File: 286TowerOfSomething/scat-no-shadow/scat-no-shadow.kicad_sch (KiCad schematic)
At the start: 1 part, among them J1 Bus_ISA_16bit

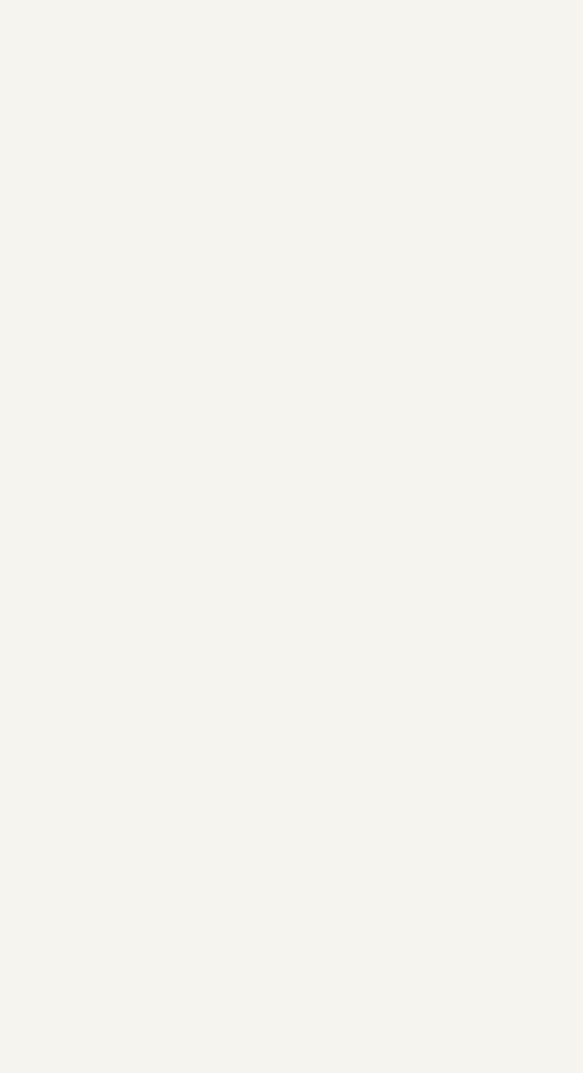
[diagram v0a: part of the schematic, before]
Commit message: Added symbol for 286 CPU, and associated datasheet
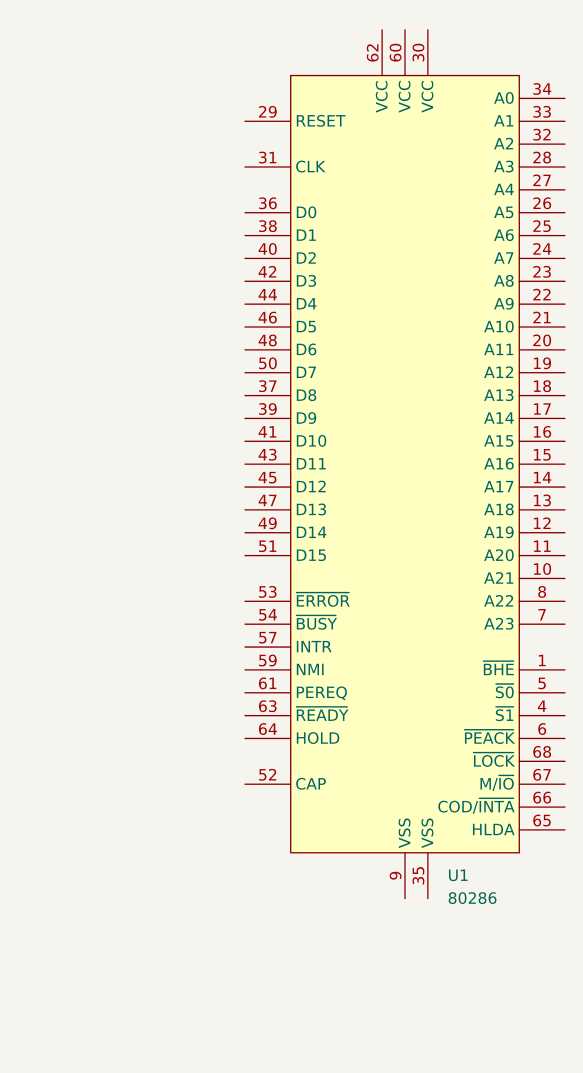
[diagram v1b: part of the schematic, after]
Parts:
- added U1: 80286, Package_LCC:PLCC-68_THT-Socket, symbol pc-parts:80286
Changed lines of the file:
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@@
 	(paper "A4")
+	(symbol
+		(lib_id "pc-parts:80286")
+		(at 129.54 86.36 0)
+		(unit 1)
+		(exclude_from_sim no)
+		(in_bom yes)
+		(on_board yes)
+		(dnp no)
+		(fields_autoplaced yes)
+		(property "Reference" "U1"
+			(at 134.2741 132.08 0)
+			(effects
+				(font
+					(size 1.27 1.27)
+				)
+				(justify left)
+			)
+		)
+		(property "Value" "80286"
+			(at 134.2741 134.62 0)
+			(effects
+				(font
+					(size 1.27 1.27)
+				)
+				(justify left)
+			)
+		)
+		(property "Footprint" "Package_LCC:PLCC-68_THT-Socket"
+			(at 129.54 86.36 0)
+			(effects
+				(font
+					(size 1.27 1.27)
+				)
+				(hide yes)
+			)
+		)
+		(property "Datasheet" ""
+			(at 129.54 86.36 0)
+			(effects
+				(font
+					(size 1.27 1.27)
+				)
+				(hide yes)
+			)
+		)
+		(property "Description" ""
+			(at 129.54 86.36 0)
+			(effects
+				(font
+					(size 1.27 1.27)
+				)
+				(hide yes)
+			)
+		)
+		(pin "59"
+		)
+		(pin "29"
+		)
+		(pin "44"
+		)
+		(pin "65"
+		)
+		(pin "38"
+		)
+		(pin "27"
+		)
+		(pin "6"
+		)
+		(pin "5"
+		)
+		(pin "51"
+		)
+		(pin "52"
+		)
+		(pin "53"
+		)
+		(pin "12"
+		)
+		(pin "40"
+		)
+		(pin "26"
+		)
+		(pin "9"
+		)
+		(pin "48"
+		)
+		(pin "34"
+		)
+		(pin "68"
+		)
+		(pin "37"
+		)
+		(pin "8"
+		)
+		(pin "62"
+		)
+		(pin "20"
+		)
+		(pin "64"
+		)
+		(pin "54"
+		)
+		(pin "4"
+		)
+		(pin "61"
+		)
+		(pin "63"
+		)
+		(pin "35"
+		)
+		(pin "66"
+		)
+		(pin "43"
+		)
+		(pin "46"
+		)
+		(pin "7"
+		)
+		(pin "57"
+		)
+		(pin "30"
+		)
+		(pin "32"
+		)
+		(pin "45"
+		)
+		(pin "36"
+		)
+		(pin "50"
+		)
+		(pin "39"
+		)
+		(pin "24"
+		)
+		(pin "18"
+		)
+		(pin "28"
+		)
+		(pin "17"
+		)
+		(pin "31"
+		)
+		(pin "60"
+		)
+		(pin "21"
+		)
+		(pin "33"
+		)
+		(pin "23"
+		)
+		(pin "25"
+		)
+		(pin "19"
+		)
+		(pin "22"
+		)
+		(pin "15"
+		)
+		(pin "11"
+		)
+		(pin "10"
+		)
+		(pin "16"
+		)
+		(pin "41"
+		)
+		(pin "1"
+		)
+		(pin "13"
+		)
+		(pin "47"
+		)
+		(pin "49"
+		)
+		(pin "42"
+		)
+		(pin "14"
+		)
+		(pin "67"
+		)
+		(instances
+			(project ""
+				(path "/1307a1c5-eee1-43f5-b6e9-638f413fecd9"
+					(reference "U1")
+					(unit 1)
+				)
+			)
+		)
+	)
 	(symbol
 		(lib_id "Connector:Bus_ISA_16bit")

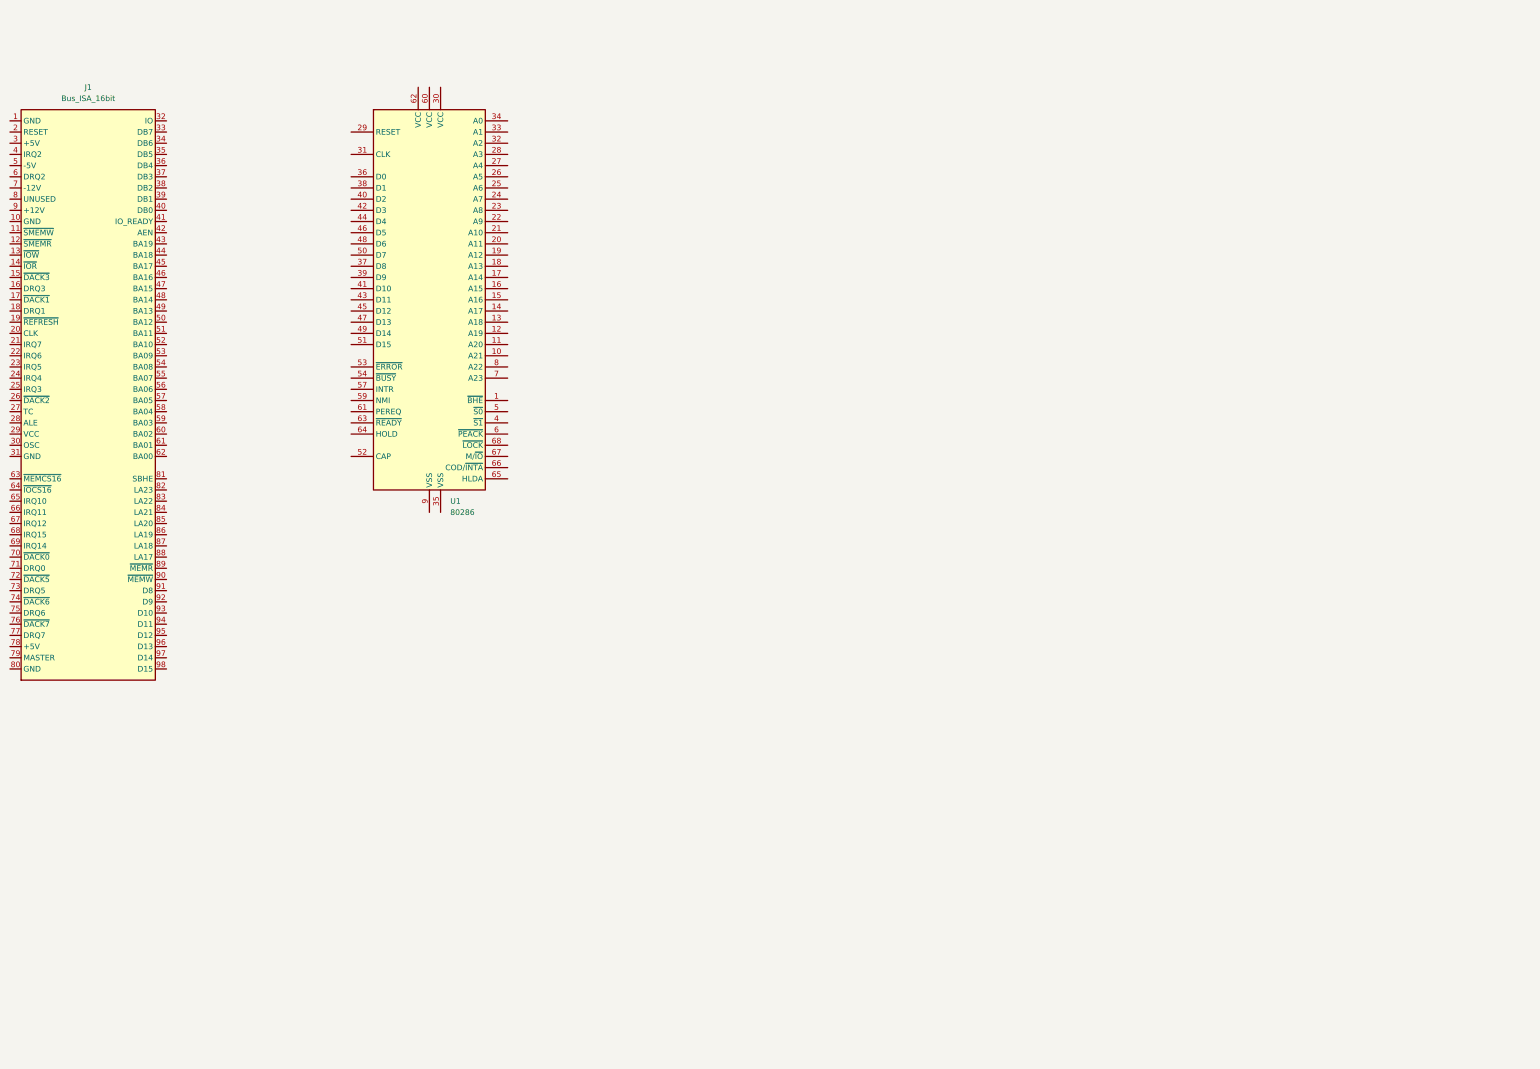
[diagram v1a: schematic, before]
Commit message: Started adding more parts to 286 card
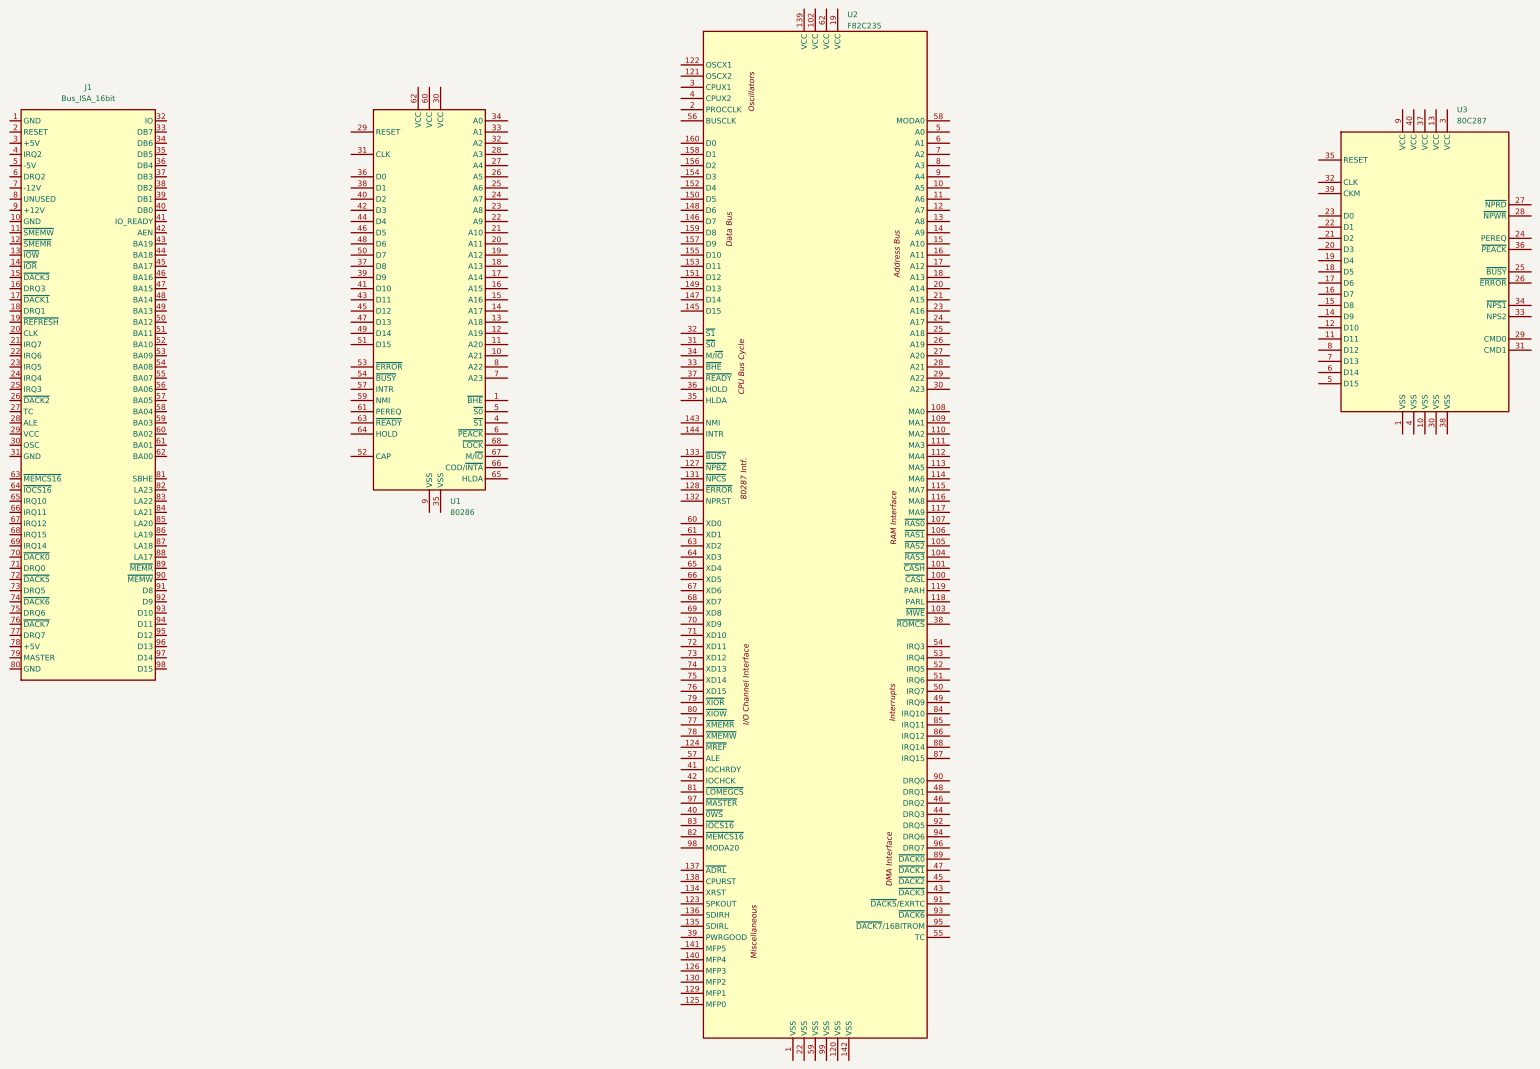
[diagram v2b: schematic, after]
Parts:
- added U2: F82C235, Package_QFP:PQFP-160_28x28mm_P0.65mm, symbol pc-parts:F82C235
- added U3: 80C287, Package_DIP:DIP-40_W15.24mm, symbol pc-parts:80C287
